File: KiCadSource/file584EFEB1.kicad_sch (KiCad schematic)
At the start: 57 parts, among them J2 SIL6, U12 XC7A35T-FTG256

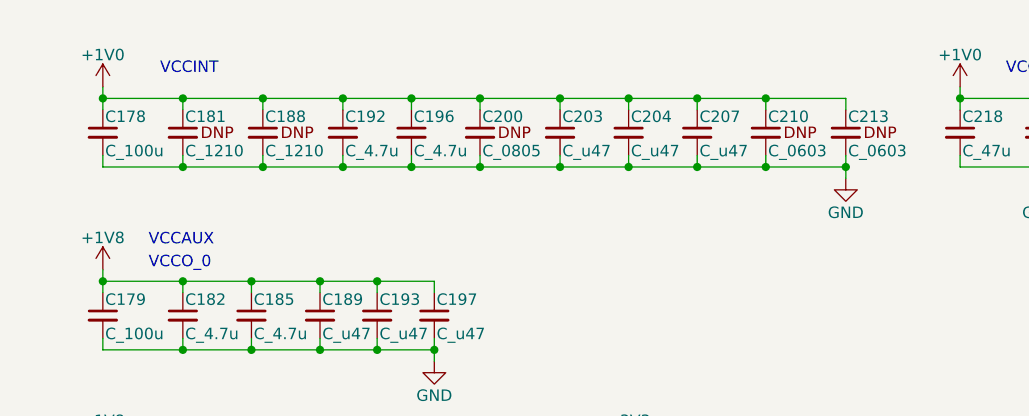
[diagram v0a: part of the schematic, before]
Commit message: updating part attributes
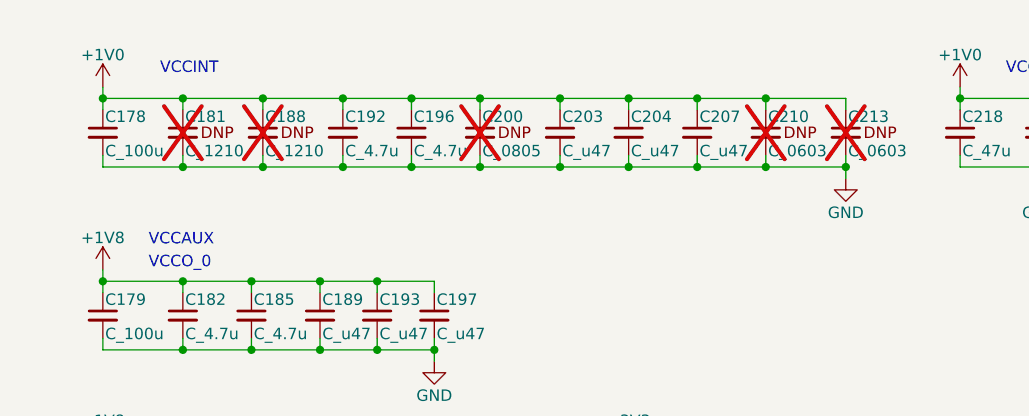
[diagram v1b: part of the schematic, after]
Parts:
- C181, C188, C200, C210, C213: now not fitted
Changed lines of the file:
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@@
 		(in_bom yes)
 		(on_board yes)
-		(dnp no)
+		(dnp yes)
 		(property "Reference" "C181"
 			(at 53.594 35.052 0)
@@
 		(in_bom yes)
 		(on_board yes)
-		(dnp no)
+		(dnp yes)
 		(property "Reference" "C188"
 			(at 62.484 35.052 0)
@@
 		(in_bom yes)
 		(on_board yes)
-		(dnp no)
+		(dnp yes)
 		(property "Reference" "C200"
 			(at 86.614 35.052 0)
@@
 		(in_bom yes)
 		(on_board yes)
-		(dnp no)
+		(dnp yes)
 		(property "Reference" "C210"
 			(at 118.364 35.052 0)
@@
 		(in_bom yes)
 		(on_board yes)
-		(dnp no)
+		(dnp yes)
 		(property "Reference" "C213"
 			(at 127.254 35.052 0)
